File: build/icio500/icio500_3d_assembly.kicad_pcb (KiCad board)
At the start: 4 copper layers, 147.6 x 105 mm, 57 parts, among them J1 ?, U1 ?, U2 ?, U3 ?, U4 ?, U5 ?, U6 ?

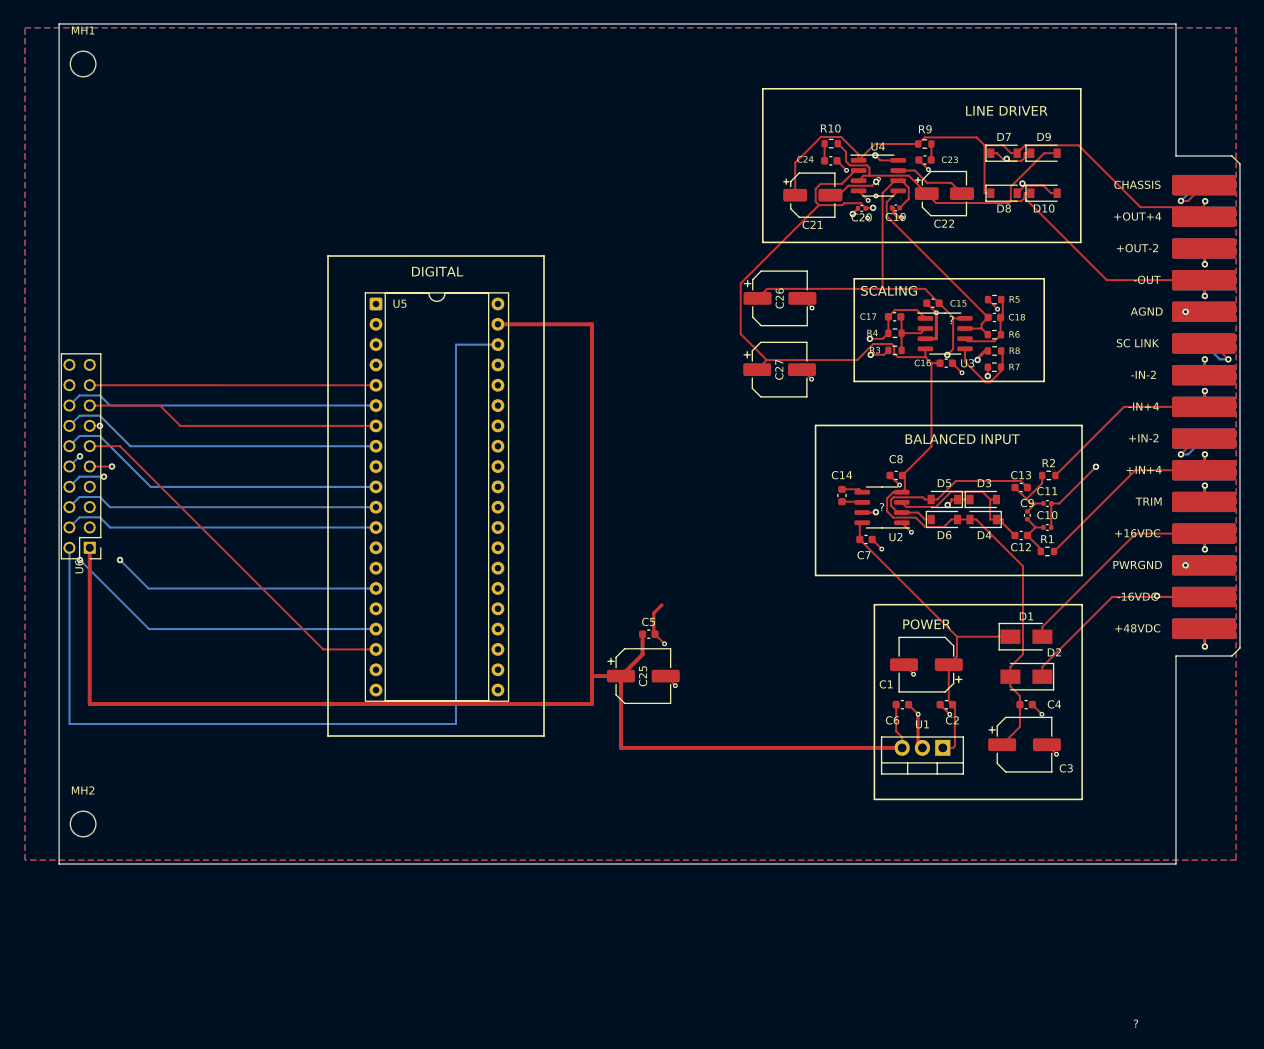
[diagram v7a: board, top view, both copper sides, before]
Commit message: Finalize VPR-500 mechanical mating, zero-DRC routing, unit 3D model scale, and JLCPCB packages
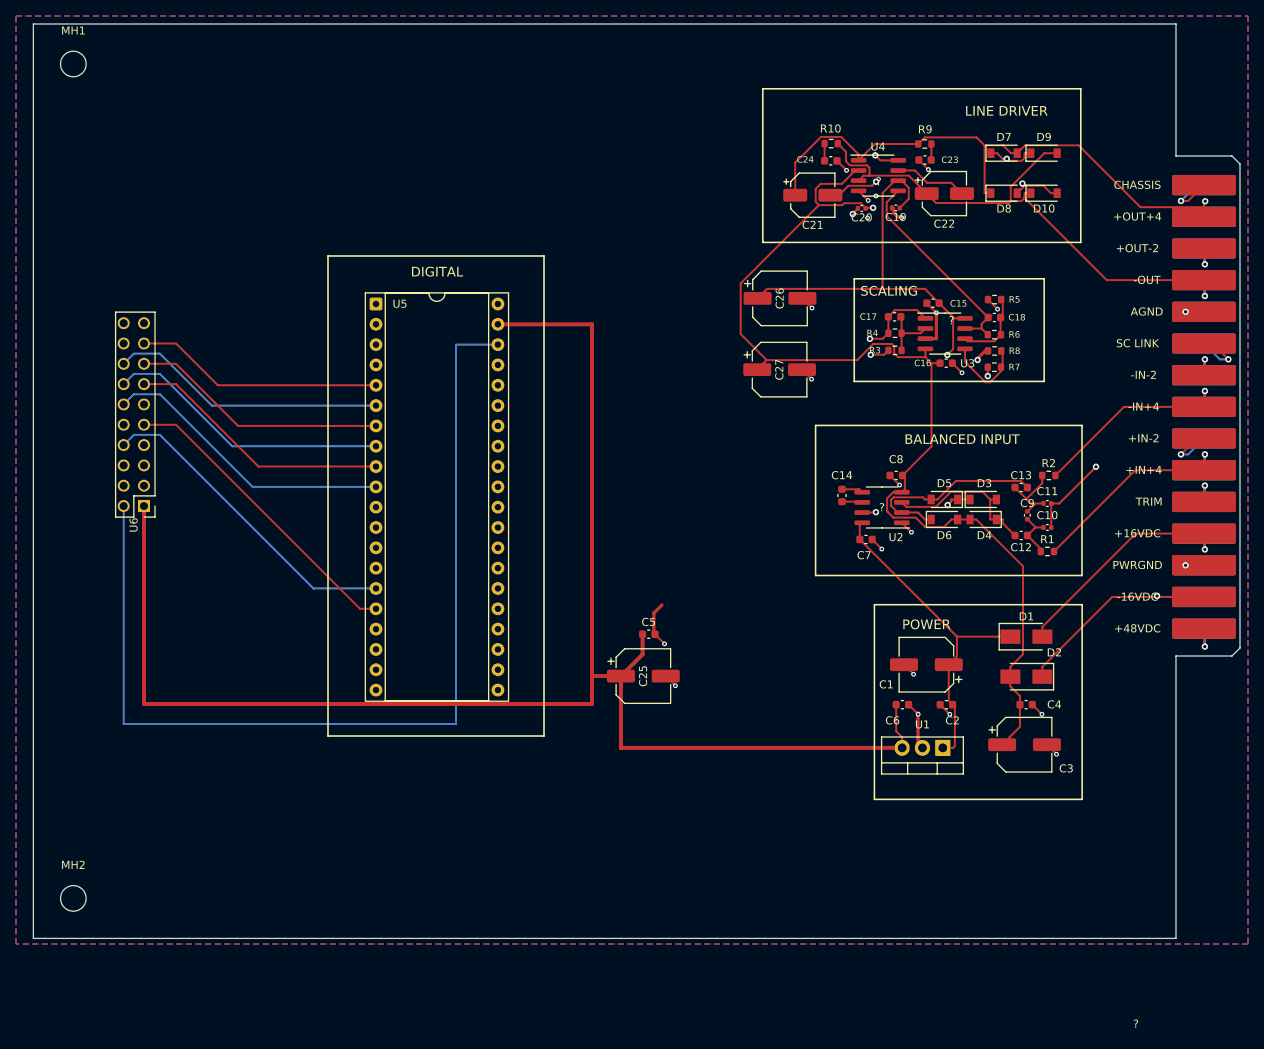
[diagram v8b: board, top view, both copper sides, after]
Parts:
- removed the ? at (55.4, 112.2)
- added ?: , DUMMY_ASSEMBLY, F.Cu at (52.2, 112.2)
- moved MH2 9.38 mm to (57.2, 164.3)
- moved U6 8.55 mm to (66.0, 115.3)
- moved MH1 1.22 mm to (57.2, 60.0)
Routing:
- net gpio_enc_sw: track 46.3 -> 80.4 mm
- net gpio_enc_b: track 55.4 -> 69.0 mm, vias 2 -> 0
- net d13: track 50.7 -> 40.0 mm, vias 2 -> 0
- net d14: track 47.6 -> 38.5 mm, vias 1 -> 0
- net i2c1_scl: track 39.4 -> 34.8 mm
- net gpio_disp_dc: track 39.4 -> 34.8 mm
- net i2c1_sda: track 39.4 -> 34.8 mm
- net spi1_sck: track 40.4 -> 35.8 mm
- net spi1_mosi: track 41.5 -> 36.9 mm
- net spi1_miso: track 37.9 -> 33.3 mm, vias 1 -> 0
- net spi1_cs: track 36.8 -> 32.2 mm
- net gpio_disp_res: track 35.8 -> 31.2 mm
- net audio_in_r: track 123.0 -> 121.4 mm
- net daisy_5v_power: track 201.3 -> 199.8 mm
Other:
- board size 147.6 x 105 mm -> 150.8 x 114.3 mm
